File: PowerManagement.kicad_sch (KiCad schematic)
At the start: 54 parts, among them J20 Conn_01x05, J4 Conn_02x03_Odd_Even, J5 BATT1_jmp, J6 BATT2_jmp, Q3 IRLZ44NSTRL(UMW), Q4 IRLZ44NSTRL(UMW), Q6 2N7002, Q7 BSS223PW, U3 MAX17320G20+T

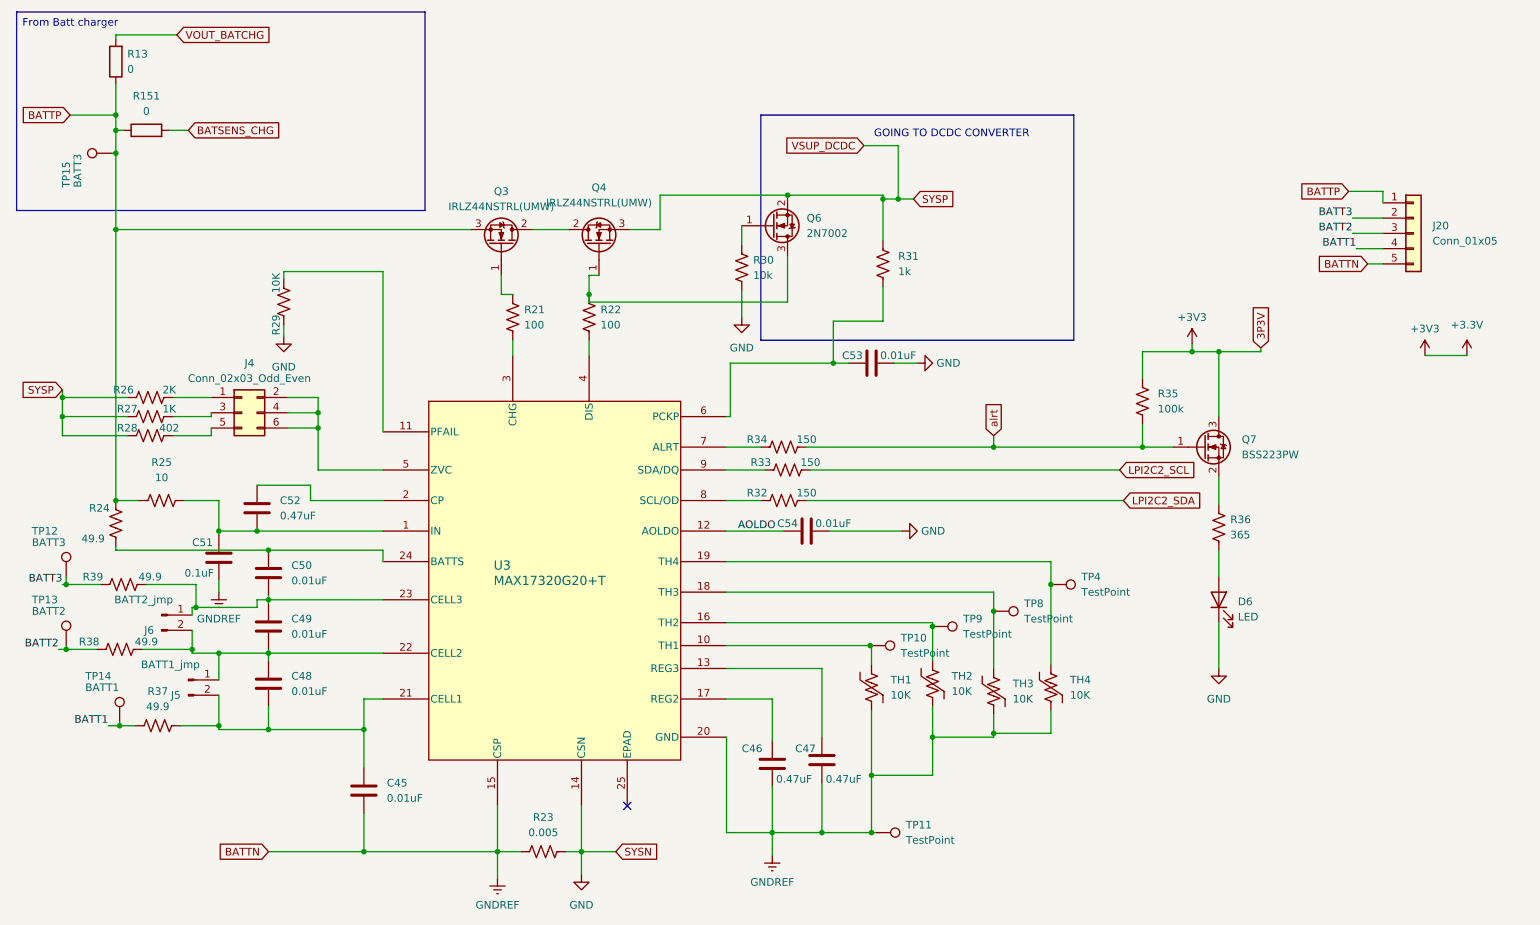
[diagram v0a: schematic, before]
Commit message: add revision to motor
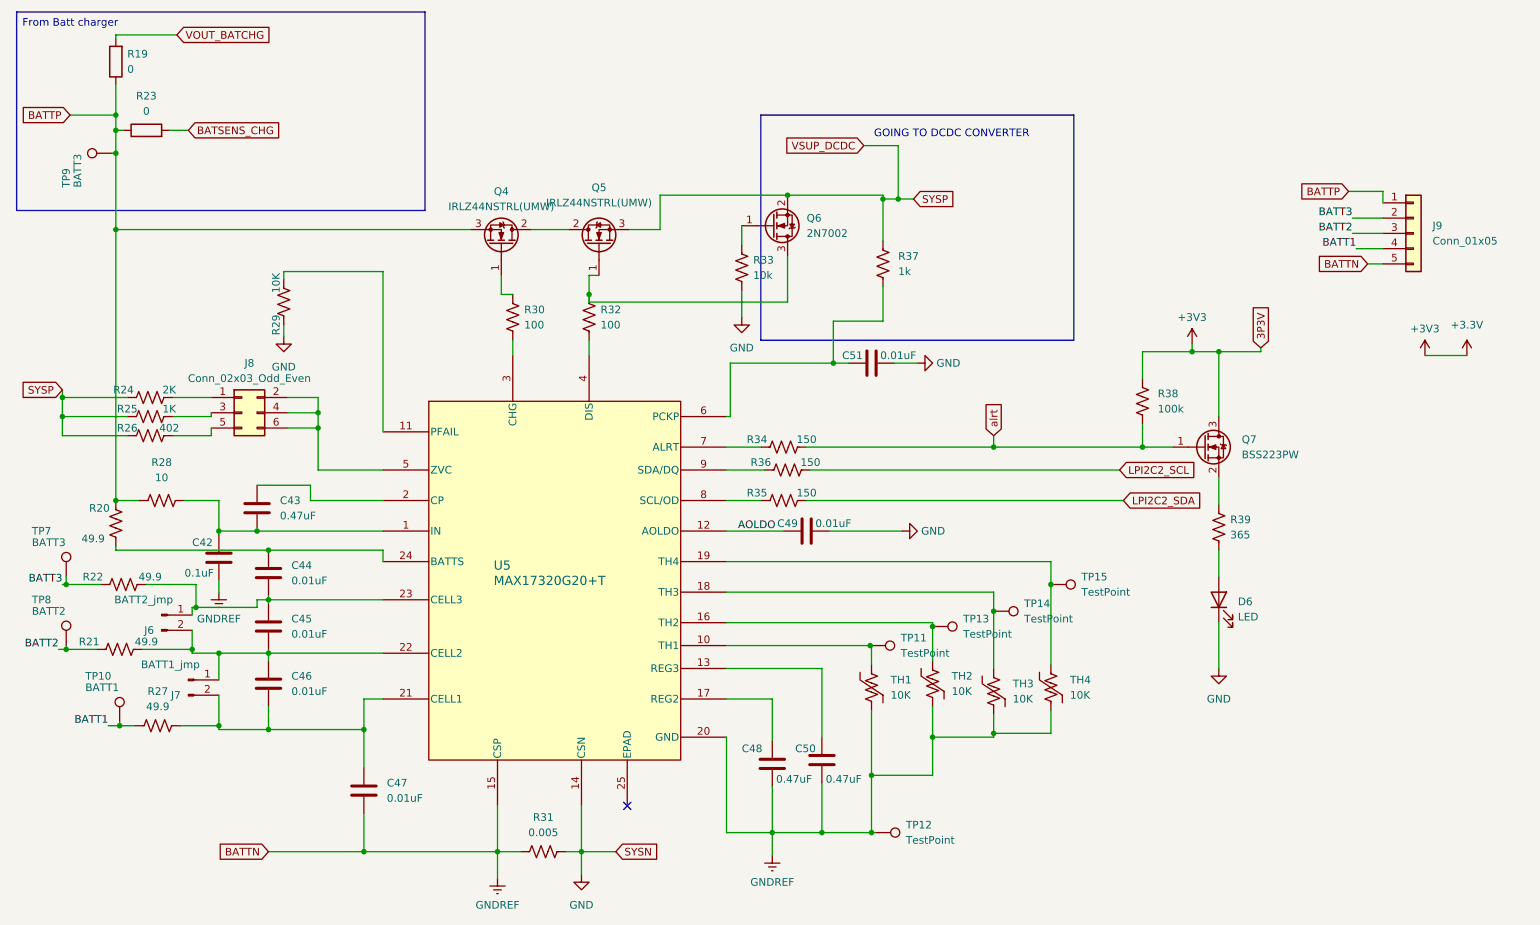
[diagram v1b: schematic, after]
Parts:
- renumbered C51 to C42, C52 to C43, C50 to C44, C49 to C45, C48 to C46, C45 to C47, C46 to C48, C54 to C49, C47 to C50, C53 to C51, J5 to J7, J4 to J8, J20 to J9, Q3 to Q4, Q4 to Q5, R13 to R19, R24 to R20, R38 to R21, R39 to R22, R151 to R23, R26 to R24, R27 to R25, R28 to R26, R37 to R27, R25 to R28, R21 to R30, R23 to R31, R22 to R32, R30 to R33, R32 to R35, R33 to R36, R31 to R37, R35 to R38, R36 to R39, TP14 to TP10, TP10 to TP11, TP11 to TP12, TP9 to TP13, TP8 to TP14, TP4 to TP15, TP12 to TP7, TP13 to TP8, TP15 to TP9, U3 to U5

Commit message: del some
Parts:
- removed J9: Conn_01x05, Connector_PinSocket_2.54mm:PinSocket_1x05_P2.54mm_Vertical, symbol Connector_Generic:Conn_01x05
- added J10: Conn_01x06, Connector_PinSocket_2.54mm:PinSocket_1x06_P2.54mm_Vertical, symbol Connector_Generic:Conn_01x06
- added J6: BATT2_jmp, Connector_PinHeader_2.54mm:PinHeader_1x02_P2.54mm_Vertical, symbol Connector:Conn_01x02_Pin
- renumbered J6 to J7, J7 to J8, J8 to J9
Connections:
- net BATT1: now also J10.5 (Pin_5)
- net BATT2: now also J10.4 (Pin_4)
- net BATT3: now also J10.3 (Pin_3)
- net BATTP: now also J10.1 (Pin_1), J10.2 (Pin_2)
- net GNDREF: now also J10.6 (Pin_6)
- net at C44.2, C45.1, J7.1 (Pin_1)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: now also J6.2 (Pin_2)
- net at C44.1, R20.2, U5.24 (BATTS): now also J6.1 (Pin_1)

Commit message: dad
da
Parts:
- C42: value 0.1uF -> 100nF; Manufacturer_Part_Number (none) -> CS1005X7R104K500NR
- C43, C48, C50: value 0.47uF -> 470nF; Manufacturer_Part_Number (none) -> GRM155R61H474KE11D
- C44, C45, C46, C47, C49, C51: value 0.01uF -> 10nF; Manufacturer_Part_Number (none) -> CC0402KRX7R9BB103
- D6: Manufacturer_Part_Number (none) -> C6210741
- J10, J6, J7, J8, J9, TP10, TP11, TP12, TP13, TP14, TP15, TP7, TP8, TP9: now not fitted
- Q4, Q5: Manufacturer_Part_Number (none) -> IRLZ44NSTRL(UMW)
- Q6: Manufacturer_Part_Number (none) -> 2N7002,215
- Q7: Manufacturer_Part_Number (none) -> BSS223PW-VB
- R19, R23: Manufacturer_Part_Number (none) -> RC0402FR-070RL
- R20, R21, R22, R27: Manufacturer_Part_Number (none) -> 0402WGF499JTCE
- R24: Manufacturer_Part_Number (none) -> 0402WGF2001TCE
- R25: Manufacturer_Part_Number (none) -> 0402WGF1001TCE
- R26: Manufacturer_Part_Number (none) -> RC0402FR-07402RL
- R28: Manufacturer_Part_Number (none) -> FRC0402F10R0TS
- R29, TH1, TH2, TH3, TH4: Manufacturer_Part_Number (none) -> RC0402FR-0710KL
- R30, R32: Manufacturer_Part_Number (none) -> RC0402FR-07100RL
- R31: value 0.005 -> 0.05; Manufacturer_Part_Number (none) -> CS02W8F500MTCE
- R33: value 10k -> 10K; Manufacturer_Part_Number (none) -> RC0402FR-0710KL
- R34, R35, R36: Manufacturer_Part_Number (none) -> RC0402FR-07150RL
- R37: value 1k -> 1K; Manufacturer_Part_Number (none) -> 0402WGF1001TCE
- R38: value 100k -> 100K; Manufacturer_Part_Number (none) -> RC0402FR-07100KL
- R39: Manufacturer_Part_Number (none) -> RC-02K3650FT
- U5: Manufacturer_Part_Number (none) -> MAX17320G20+T

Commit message: gema
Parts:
- removed R19, R23: 0, Resistor_SMD:R_0402_1005Metric, symbol Device:R
- C42:  LCSC Part # (none) -> C77020; Manufacturer_Part_Number CS1005X7R104K500NR -> GRM155R71H104KE14D
- C43, C48, C50:  LCSC Part # (none) -> C437527
- C44, C45, C46, C47, C49, C51:  LCSC Part # (none) -> C60133
- D6:  LCSC Part # (none) -> C6210741
- Q4, Q5:  LCSC Part # (none) -> C42370422
- Q6:  LCSC Part # (none) -> C65189
- Q7:  LCSC Part # (none) -> C5197341
- R20, R21, R22, R27:  LCSC Part # (none) -> C25120
- R24:  LCSC Part # (none) -> C4109
- R25, R37:  LCSC Part # (none) -> C11702
- R26:  LCSC Part # (none) -> C137984
- R28:  LCSC Part # (none) -> C2906862
- R29, R33, TH1, TH2, TH3, TH4:  LCSC Part # (none) -> C60490
- R30, R32:  LCSC Part # (none) -> C106232
- R31:  LCSC Part # (none) -> C473658
- R34, R35, R36:  LCSC Part # (none) -> C138054
- R38:  LCSC Part # (none) -> C60491
- R39:  LCSC Part # (none) -> C453662
- U5:  LCSC Part # (none) -> C7457895
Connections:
- net SYSP is gone; now on net BATSENS_CHG: Q5.3 (S), Q6.2 (S), R24.1, R25.1, R26.1, R37.1
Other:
- note added: "From Charger"
- note removed: "GOING TO DCDC CONVERTER"
